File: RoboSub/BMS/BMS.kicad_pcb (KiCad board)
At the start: 2 copper layers, 127 x 50.8 mm, 40 parts, among them J1 battery, J2 temp, J3 ExtPwrSw, J4 output, J5 CAN, J6 SWD_UART, K1 A31CSP12VDC2D, Q1 PMV28ENEA, SW1 DBG2, SW2 DBG1, SW3 RST, U1 VXO7803, U2 CZ3A07, U3 STM32G0B1KxTxN, U4 TCAN330G, U5 PCC

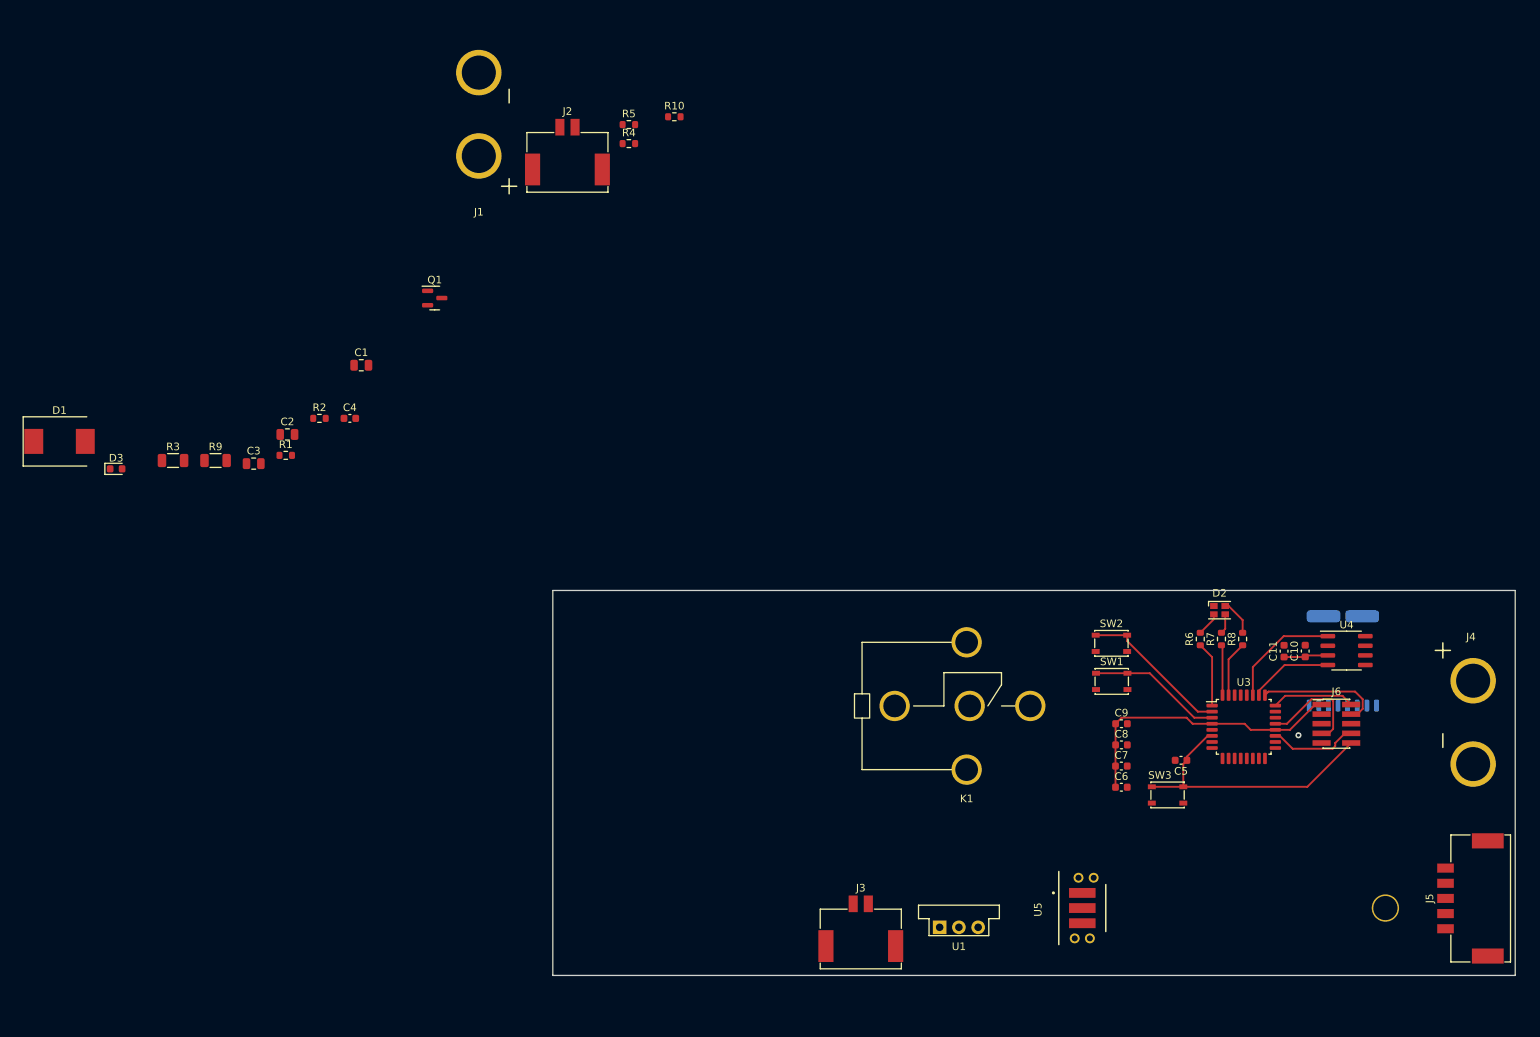
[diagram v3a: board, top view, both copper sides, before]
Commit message: Finished Layout for the BMS
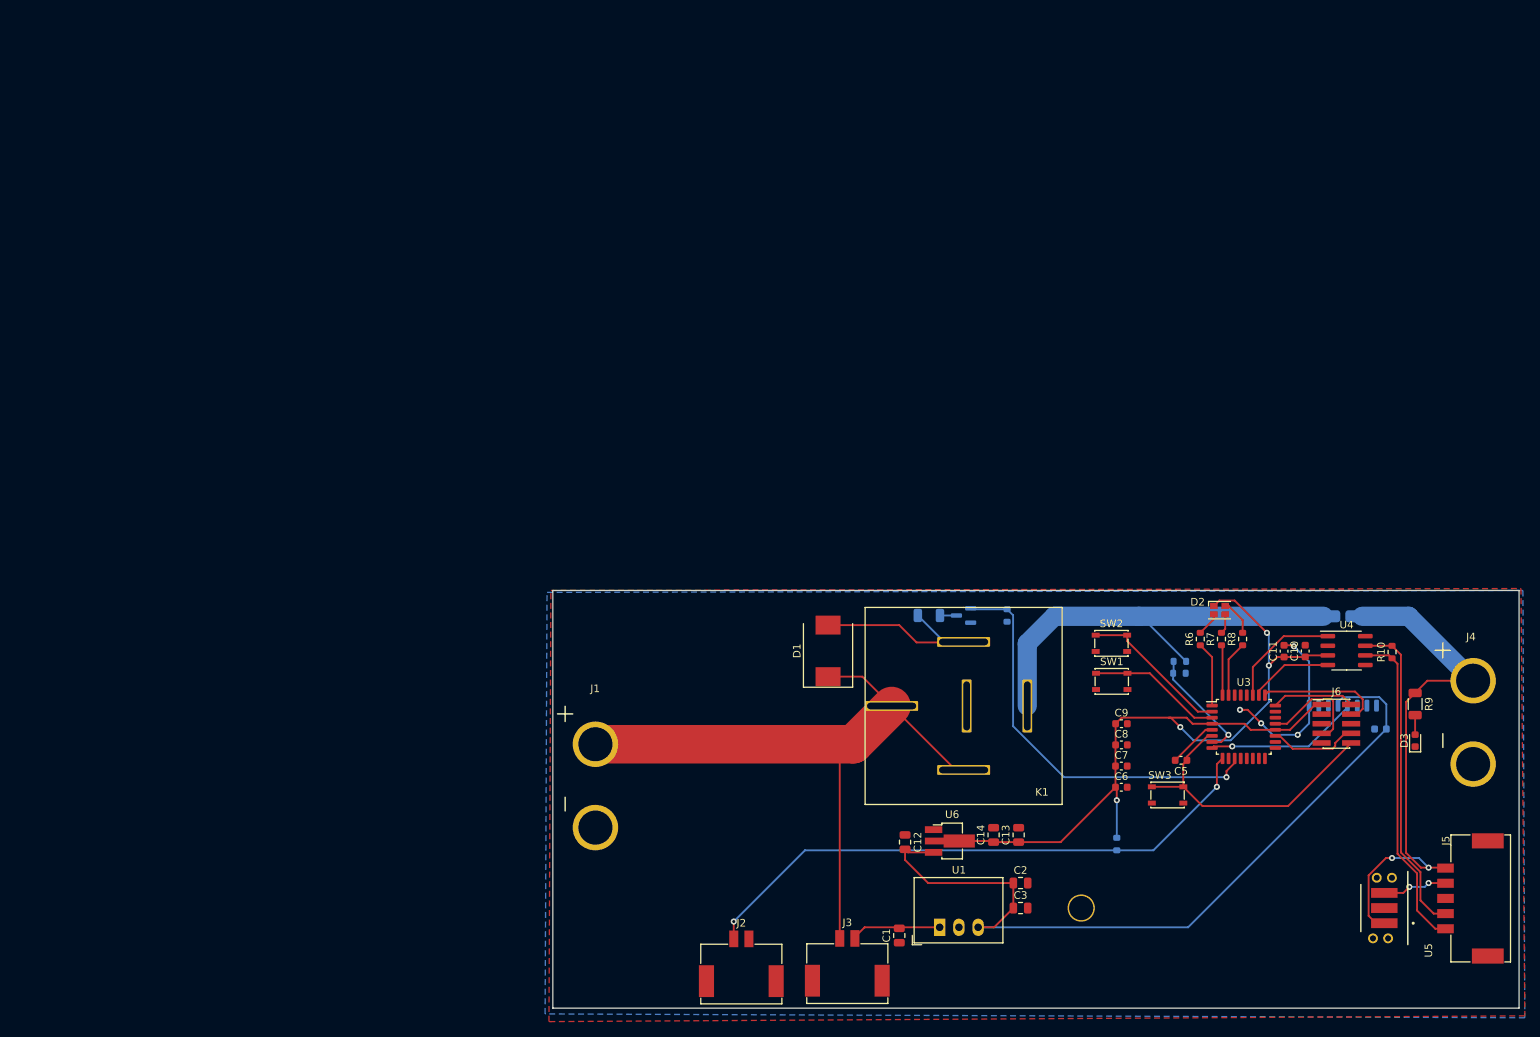
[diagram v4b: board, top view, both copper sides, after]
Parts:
- added C12: 10u, Capacitor_SMD:C_0805_2012Metric, F.Cu at (132.1, 122.6)
- added C13: 10u, Capacitor_SMD:C_0805_2012Metric, F.Cu at (147.1, 121.7)
- added C14: 10u, Capacitor_SMD:C_0805_2012Metric, F.Cu at (143.8, 121.7)
- added U6: AZ1117-3.3, Package_TO_SOT_SMD:SOT-89-3_Handsoldering, F.Cu at (138.0, 122.5)
- C4, Q1, R1, R2, R3, R4, R5: moved to B.Cu
- K1: value A31CSP12VDC2D -> A3M1CSQ12VDC2; footprint BMS_Library:A3_Relay -> BMS_Library:A3M1CSQ12VDC2
- U1: value VXO7803 -> R-785.0-1.0; footprint Converter_DCDC:Converter_DCDC_Murata_OKI-78SR_Vertical -> Converter_DCDC:Converter_DCDC_RECOM_R-78E-0.5_THT
- moved D3 175.1 mm to (199.4, 109.2), turned to 90 degrees
- moved R9 161.5 mm to (199.4, 104.4), turned to -90 degrees
- moved C4 142.0 mm to (194.8, 107.7), turned to 180 degrees
- moved R1 121.1 mm to (160.0, 122.9), turned to -90 degrees
- moved R10 118.1 mm to (196.3, 97.5), turned to 90 degrees
- moved C3 117.0 mm to (147.3, 131.3)
- moved C2 113.4 mm to (147.3, 128.0)
- moved J2 109.5 mm to (110.5, 144.0)
- moved D1 105.1 mm to (121.9, 97.4), turned to 90 degrees
- moved C1 103.5 mm to (131.3, 134.9), turned to 90 degrees
- moved R5 102.6 mm to (168.3, 100.3)
- moved R3 101.8 mm to (135.2, 92.7), turned to 180 degrees
- moved R4 99.8 mm to (168.3, 98.8), turned to 180 degrees
- moved R2 94.4 mm to (145.5, 92.7), turned to 90 degrees
- moved Q1 81.4 mm to (139.8, 92.7), turned to 180 degrees
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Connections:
- C2 pad 1: +3V3 -> +5V
- C3 pad 1: +3V3 -> +5V
- C4 pad 1: +3V3 -> +5V
- U1 pad 3: +3V3 -> +5V
- U2 pad 13: +3V3 -> +5V
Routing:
- net +5V: track 0.00 -> 105.4 mm
- net +BATT: track 0.00 -> 90.5 mm
- net /T_sense: track 0.00 -> 77.5 mm, vias 0 -> 2
- net VBUS: track 0.00 -> 71.3 mm, vias 0 -> 2
- net +3V3: track 43.8 -> 114.8 mm, vias 0 -> 4
- net /VRAW: track 0.00 -> 57.5 mm
- net /enable: track 0.00 -> 54.5 mm, vias 0 -> 1
- net /CAN/CANL: track 0.00 -> 43.1 mm
- net /CAN/CANH: track 0.00 -> 42.7 mm
- net GND: track 0.00 -> 30.0 mm, vias 0 -> 4
- net Net-(D1-Pad2): track 0.00 -> 26.4 mm
- net /I_sense: track 0.00 -> 20.3 mm, vias 0 -> 1
- net /V_sense: track 0.00 -> 15.3 mm, vias 0 -> 1
- net Net-(C1-Pad2): track 0.00 -> 12.0 mm
- net /PCC_3V3: track 0.00 -> 8.63 mm, vias 0 -> 2
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- added copper zone on B.Cu, net GND
- added copper zone on F.Cu, net GND
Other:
- board size 127 x 50.8 mm -> 127.5 x 55.1 mm

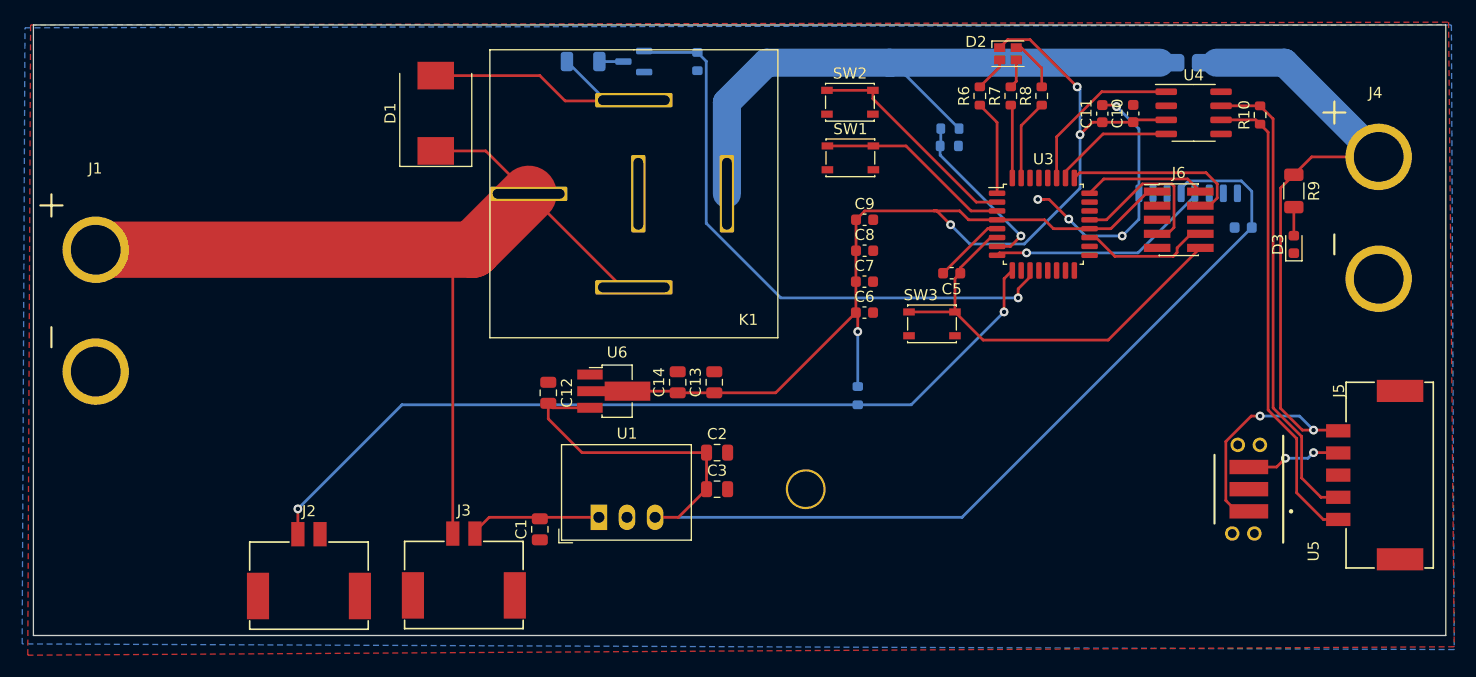
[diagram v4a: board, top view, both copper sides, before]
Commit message: created zones for the BAT, VRAW, VBUS and moved STM32 to back of board
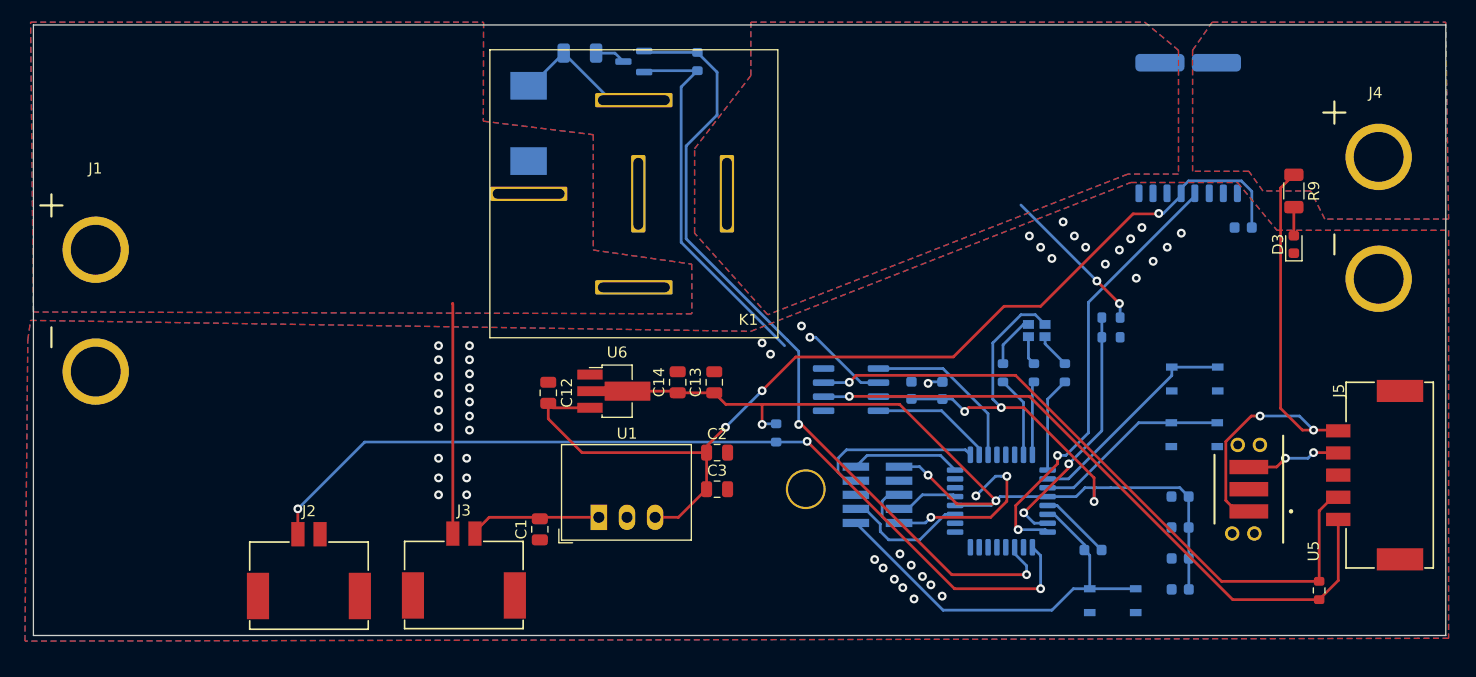
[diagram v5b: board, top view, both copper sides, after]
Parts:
- C10, C11, C5, C6, C7, C8, C9, D1, D2, J6, R6, R7, R8, SW1, SW2, SW3, U3, U4: moved to B.Cu
- moved R10 43.3 mm to (201.7, 140.5)
- moved SW2 39.9 mm to (190.4, 121.4), turned to 180 degrees
- moved SW1 39.9 mm to (190.4, 126.4), turned to 180 degrees
- moved U4 39.8 mm to (159.4, 122.3), turned to 180 degrees
- moved C7 37.9 mm to (189.1, 137.6), turned to 180 degrees
- moved C6 37.9 mm to (189.1, 140.4), turned to 180 degrees
- moved C8 37.9 mm to (189.1, 134.8), turned to 180 degrees
- moved C9 37.9 mm to (189.1, 132.0), turned to 180 degrees
- moved J6 36.8 mm to (161.8, 131.8), turned to 180 degrees
- moved C10 32.0 mm to (164.9, 122.4)
- moved SW3 29.8 mm to (183.0, 141.4), turned to 180 degrees
- moved C11 28.9 mm to (167.7, 122.4)
- moved C5 28.1 mm to (181.3, 136.8), turned to 0 degrees
- moved R6 26.1 mm to (178.7, 120.8)
- moved U3 25.3 mm to (173.0, 132.4), turned to 180 degrees
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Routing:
- net +BATT: track 90.5 -> 20.8 mm
- net /VRAW: track 57.5 -> 13.9 mm, vias 0 -> 2
- net GND: track 30.0 -> 71.2 mm, vias 4 -> 51
- net VBUS: track 71.3 -> 44.8 mm
- net /I_sense: track 20.3 -> 40.3 mm, vias 1 -> 2
- net /enable: track 54.5 -> 73.7 mm, vias 1 -> 2
- net /CAN/CANH: track 42.7 -> 61.3 mm, vias 0 -> 1
- net /CAN/CANL: track 43.1 -> 60.3 mm, vias 0 -> 1
- net +5V: track 105.4 -> 93.7 mm, vias 0 -> 3
- net Net-(D1-Pad2): track 26.4 -> 16.3 mm
- net /NOGGIN/RX: track 14.5 -> 5.66 mm
- net +3V3: track 114.8 -> 123.0 mm, vias 4 -> 6
- net /V_sense: track 15.3 -> 23.2 mm, vias 1 -> 2
- net /T_sense: track 77.5 -> 81.4 mm, vias 2 -> 3
- net /RST: track 39.4 -> 38.0 mm
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- added copper zone on B.Cu, net +BATT
- added copper zone on F.Cu, net +BATT
- added copper zone on B.Cu, net /VRAW
- added copper zone on F.Cu, net /VRAW
- added copper zone on B.Cu, net VBUS
- added copper zone on F.Cu, net VBUS

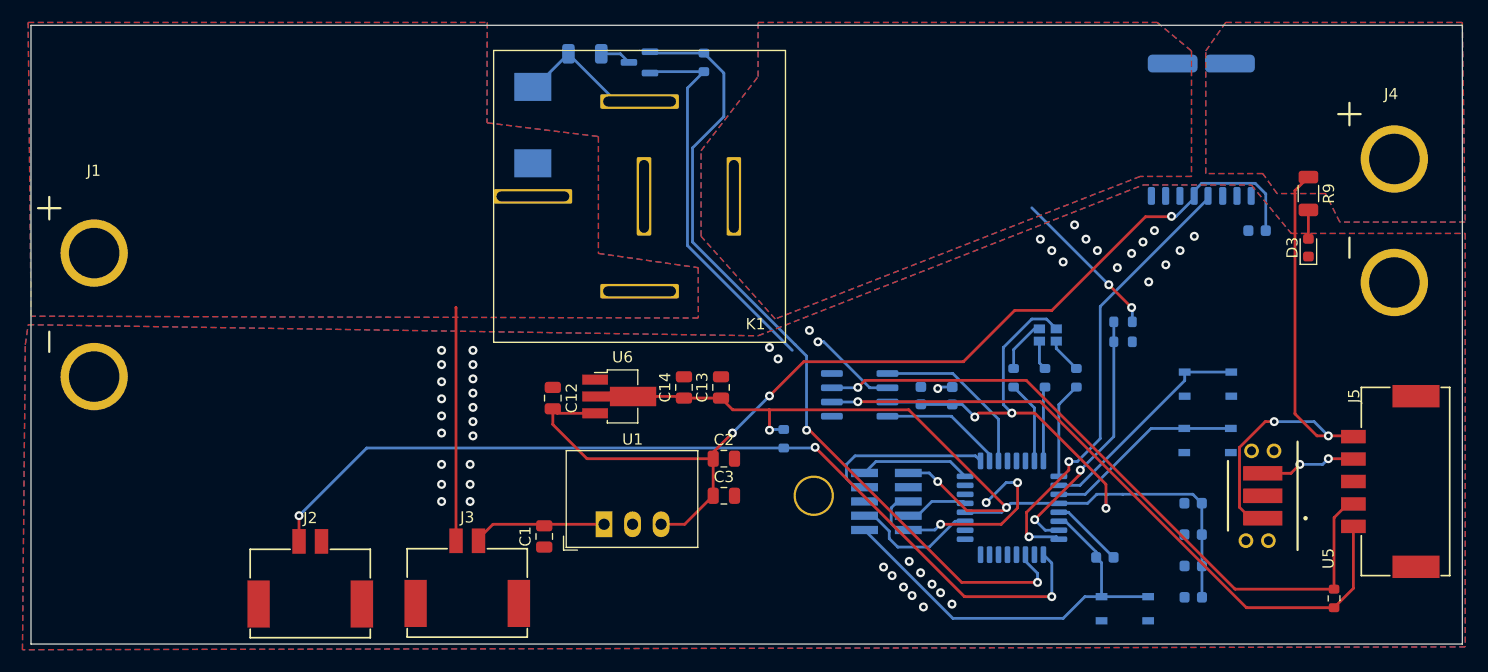
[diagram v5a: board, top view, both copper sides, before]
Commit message: compressing digital controls for better ground pour
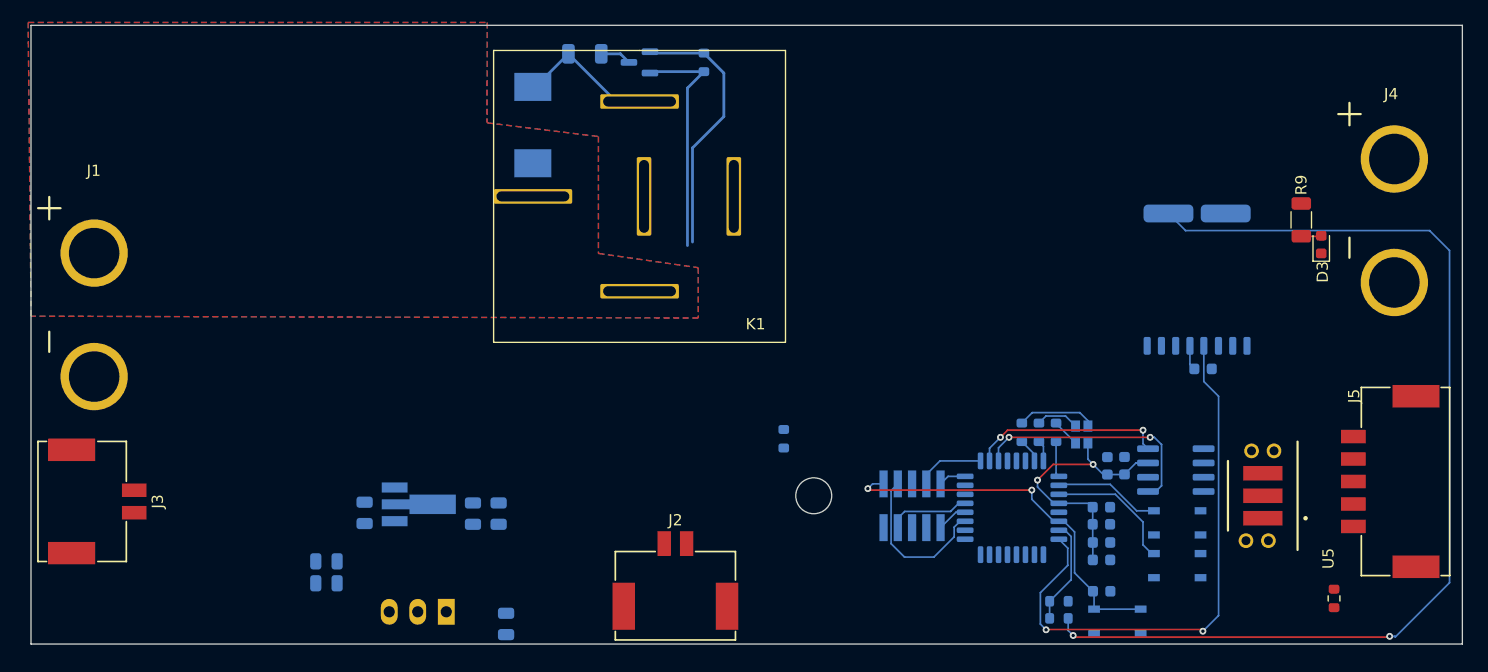
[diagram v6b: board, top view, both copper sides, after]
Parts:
- C1, C12, C13, C14, C2, C3, U1, U6: moved to B.Cu
- moved J3 40.1 mm to (86.2, 131.8), turned to -90 degrees
- moved C2 36.6 mm to (111.9, 137.2), turned to 180 degrees
- moved C3 36.3 mm to (111.9, 139.1), turned to 180 degrees
- moved J2 32.5 mm to (143.0, 144.2)
- moved U4 28.9 mm to (187.6, 129.0), turned to 0 degrees
- moved R4 27.0 mm to (177.2, 142.2)
- moved C13 24.8 mm to (125.0, 132.9)
- moved R5 23.8 mm to (177.2, 140.7)
- moved U6 20.3 mm to (120.1, 132.1)
- moved C14 20.0 mm to (127.3, 132.9)
- moved C12 19.6 mm to (115.3, 132.8), turned to 90 degrees
- moved C10 17.8 mm to (181.5, 128.7)
- moved C11 16.6 mm to (183.0, 128.6)
- moved U1 16.1 mm to (122.6, 141.7), turned to 180 degrees
- moved U2 13.4 mm to (189.5, 118.0)
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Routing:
- net +3V3: track 123.0 -> 27.1 mm, vias 6 -> 2
- net +5V: track 93.7 -> 2.21 mm, vias 3 -> 0
- net /T_sense: track 81.4 -> 0.00 mm, vias 3 -> 0
- net /VRAW: track 13.9 -> 93.3 mm
- net /CAN/CANH: track 61.3 -> 0.00 mm, vias 1 -> 0
- net /CAN/CANL: track 60.3 -> 0.00 mm, vias 1 -> 0
- net GND: track 71.2 -> 21.0 mm, vias 51 -> 0
- net /enable: track 73.7 -> 23.6 mm, vias 2 -> 0
- net VBUS: track 44.8 -> 0.00 mm, vias 2 -> 0
- net +BATT: track 20.8 -> 0.00 mm
- net /V_sense: track 23.2 -> 9.41 mm, vias 2 -> 0
- net Net-(C1-Pad2): track 12.0 -> 0.00 mm
- net /DBG1: track 20.0 -> 9.48 mm
- net /I_sense: track 40.3 -> 50.4 mm
- net /NOGGIN/SWCLK: track 15.6 -> 6.16 mm
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- removed copper zone on B.Cu, net /VRAW
- removed copper zone on F.Cu, net /VRAW
- removed copper zone on B.Cu, net GND
- removed copper zone on F.Cu, net GND
- removed copper zone on B.Cu, net VBUS
- removed copper zone on F.Cu, net VBUS

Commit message: finished update
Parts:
- moved R10 7.83 mm to (201.2, 132.7)
- moved C1 0.65 mm to (127.4, 142.4)
- moved D3 0.25 mm to (200.8, 108.9)
- moved C2 0.13 mm to (111.9, 137.0)
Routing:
- net +5V: track 2.21 -> 98.5 mm, vias 0 -> 2
- net VBUS: track 0.00 -> 77.8 mm, vias 0 -> 3
- net +3V3: track 27.1 -> 101.2 mm, vias 2 -> 5
- net /enable: track 23.6 -> 77.2 mm, vias 0 -> 4
- net /T_sense: track 0.00 -> 43.7 mm, vias 0 -> 2
- net Net-(C1-Pad2): track 0.00 -> 42.4 mm, vias 0 -> 2
- net +BATT: track 0.00 -> 26.3 mm
- net /CAN/CANL: track 0.00 -> 17.1 mm, vias 0 -> 1
- net /CAN/CANH: track 0.00 -> 14.6 mm, vias 0 -> 3
- net GND: track 21.0 -> 33.6 mm, vias 0 -> 20
- net /PCC_3V3: track 0.00 -> 8.60 mm
- net /I_sense: track 50.4 -> 51.1 mm
- added copper zone on B.Cu, net /VRAW
- added copper zone on F.Cu, net /VRAW
- added copper zone on B.Cu, net GND
- added copper zone on F.Cu, net GND
- added copper zone on B.Cu, net VBUS
- added copper zone on F.Cu, net VBUS
